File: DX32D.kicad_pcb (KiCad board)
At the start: 2 copper layers, 20.3 x 40.1 mm, 22 parts, among them J1 USB_A, J2 MicroSD Card, J3 SH I2C, SW1 reset, SW2 boot, U1 ESP32-S3-WROOM-1, U2 AMS1117-3.3

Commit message: made some small changes
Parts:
- moved SW2 0.51 mm to (154.9, 88.4)
- moved SW1 0.51 mm to (139.7, 88.4)
- moved Fiducial 0.38 mm to (138.9, 93.6)
- moved JP1 0.29 mm to (151.9, 86.5)
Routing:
- net /SD_CLK: track 16.8 -> 15.0 mm
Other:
- board text added: "32"

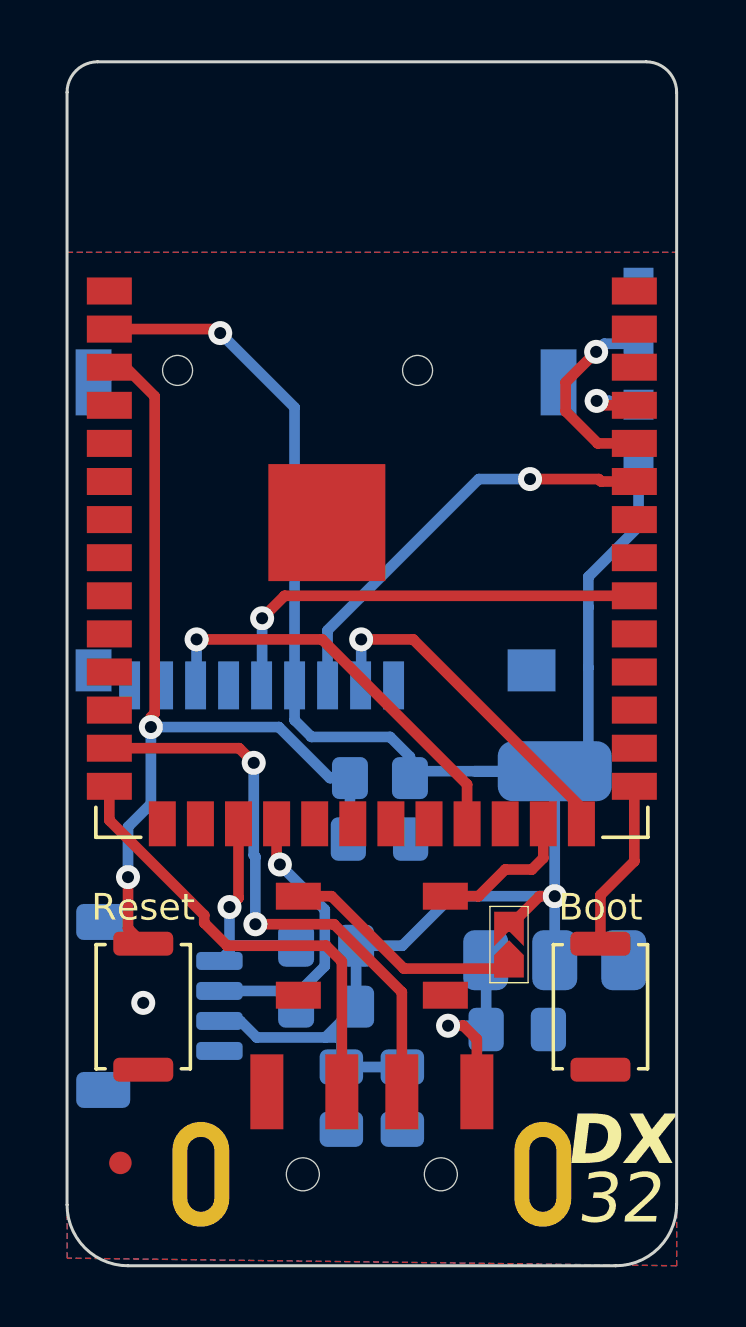
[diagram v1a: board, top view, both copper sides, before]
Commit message: updated board
changed the width of the power pads.... i should have just set a rule instead
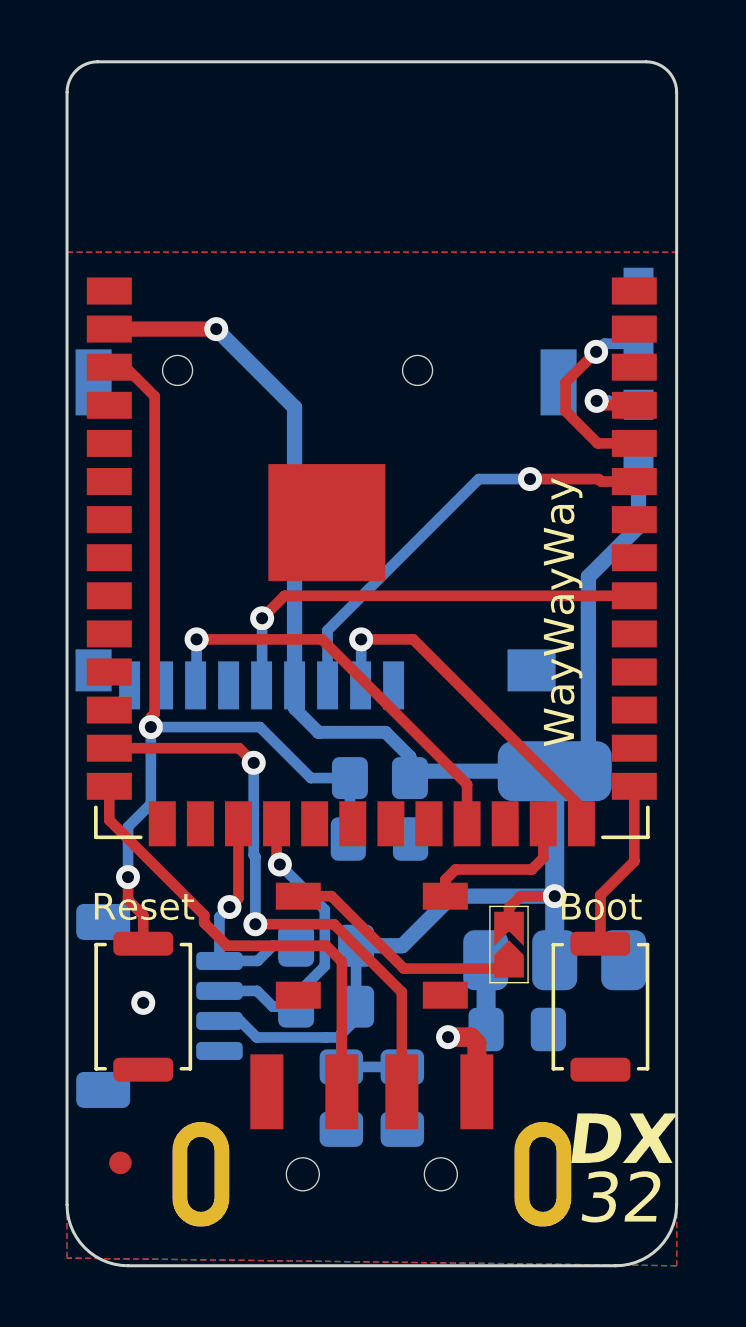
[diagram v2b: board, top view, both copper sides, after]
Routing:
- net +3.3V: track 69.1 -> 68.4 mm
- net /GPIO9_SCL: track 7.06 -> 7.60 mm
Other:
- board text added: "WayWayWay"
